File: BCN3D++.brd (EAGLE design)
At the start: 70.5 x 95.8 mm, 87 parts, among them IC2 FT232RL, Q2 IRLS3034

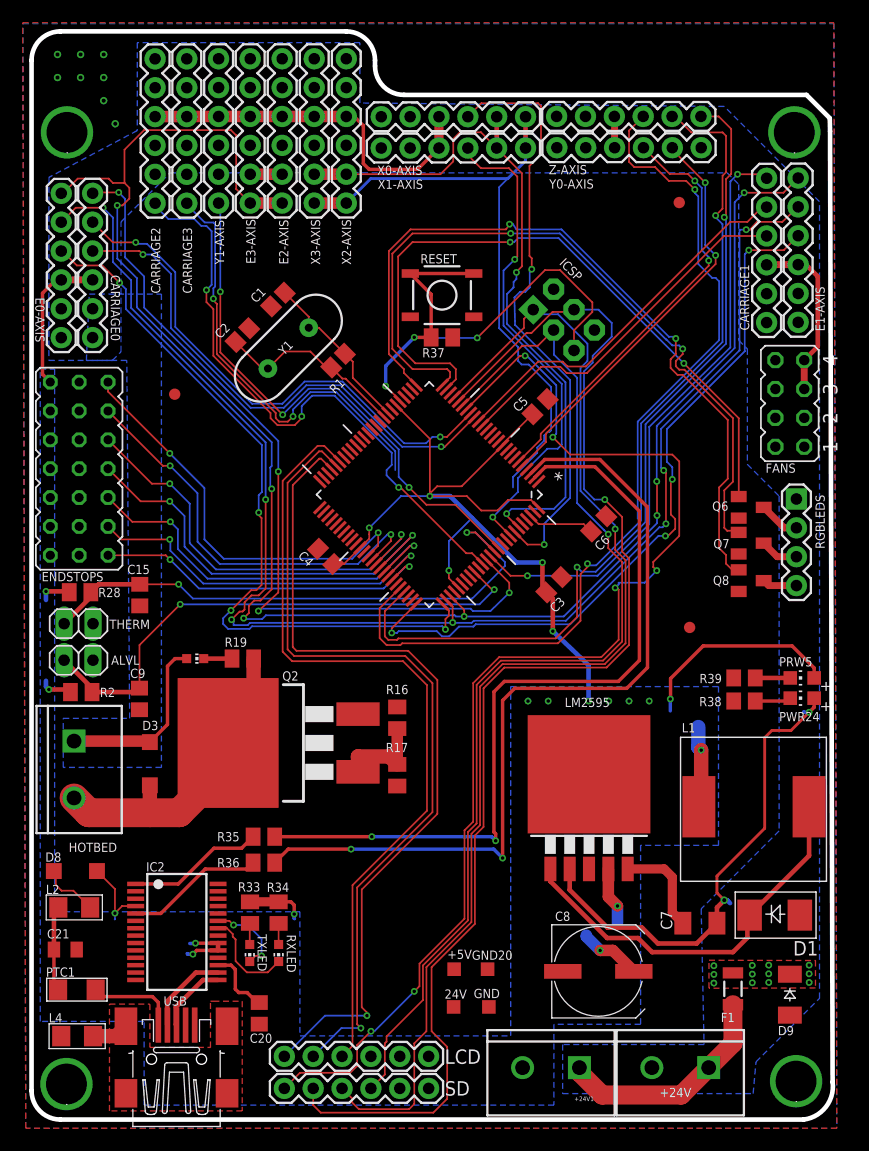
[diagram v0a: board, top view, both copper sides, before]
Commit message: Main Board almost ready
5V rail to ICSP and some headers left to connect
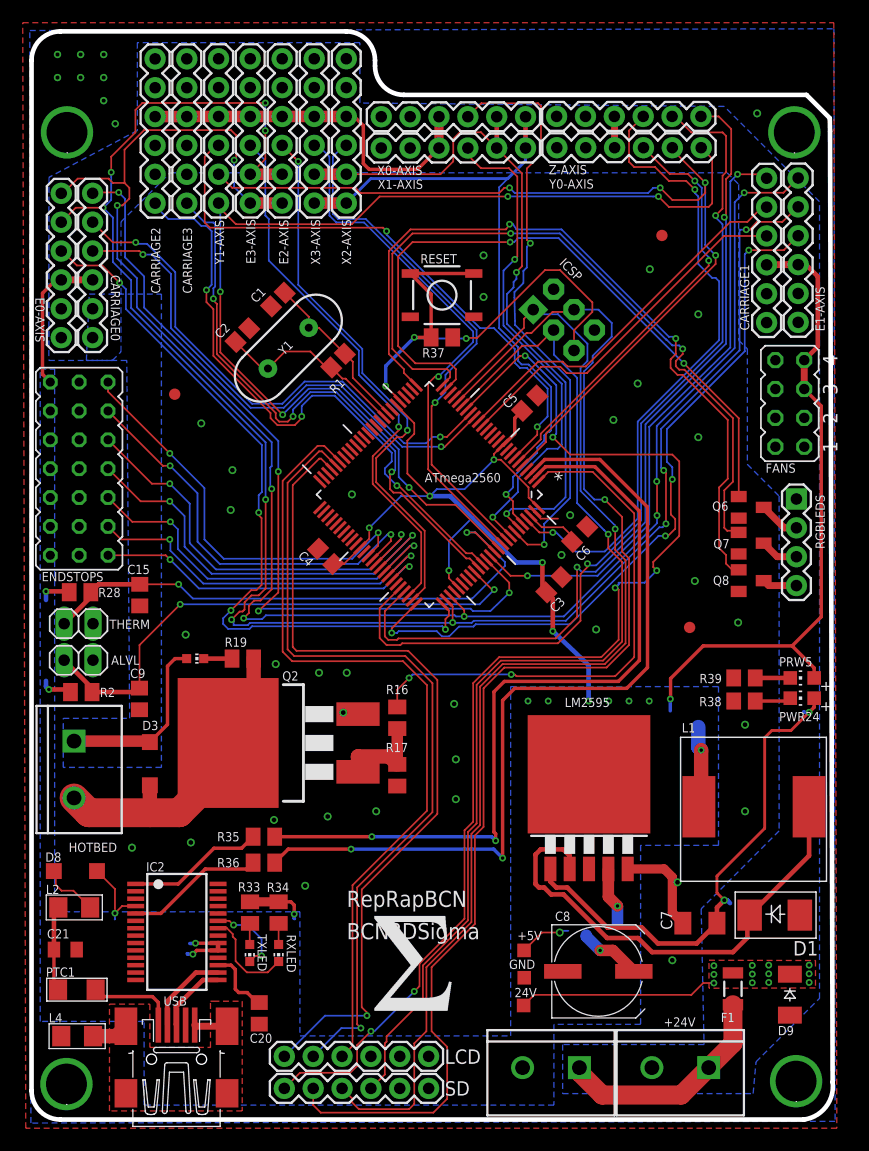
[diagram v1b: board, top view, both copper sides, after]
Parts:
- removed GND20: PTR1TP12SQ, testpad:TP12SQ
- added U$5: (no value), MarcEagleParts:SIGMA_LOGO
- moved LOGO1 63.7 mm to (27.2, 15.1)
- moved +5V 6.37 mm to (43.3, 14.9)
- moved 24V 6.16 mm to (43.3, 10.0)
- moved GND 4.03 mm to (43.4, 12.5)
- moved FID2 3.27 mm to (55.5, 77.8)
- moved C6 1.91 mm to (48.2, 51.5)
- moved C5 0.96 mm to (43.8, 63.0)
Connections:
- removed net N$128: ATMEGA2560.1
- new net 11111: ATMEGA2560.23
- net +24V: now also 24V.TP, LM2595.1; no longer LM2595.2
- net +5V: no longer 24V.TP
- net GND: no longer GND20.TP
- net N$4: now also LM2595.2; no longer LM2595.1
- net PWM_HOTBED: now also ATMEGA2560.1; no longer ATMEGA2560.23
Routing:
- net Y1-!EN: track 0.00 -> 51.8 mm, vias 0 -> 2
- net Y-STEP: track 48.1 -> 99.3 mm, vias 3 -> 5
- net E3-!EN: track 0.00 -> 48.3 mm, vias 0 -> 1
- net E2-!EN: track 0.00 -> 48.2 mm, vias 0 -> 2
- net X3-!EN: track 0.00 -> 47.0 mm, vias 0 -> 1
- net PWM_HOTBED: track 0.00 -> 46.6 mm, vias 0 -> 2
- net X2-!EN: track 0.00 -> 46.3 mm, vias 0 -> 1
- net Y-DIR: track 36.6 -> 82.3 mm, vias 2 -> 4
- net E-DIR: track 130.4 -> 158.7 mm, vias 7 -> 10
- net +5V: track 201.2 -> 226.6 mm, vias 21 -> 23
- net +24V: track 59.5 -> 78.3 mm
- net THERM3: track 38.6 -> 51.3 mm, vias 2 -> 3
- net Z-!EN: track 44.3 -> 56.4 mm, vias 1 -> 2
- net N$4: track 35.3 -> 42.6 mm
- net X-STEP: track 55.2 -> 59.3 mm, vias 0 -> 1
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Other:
- board text added: "ATmega2560"
- board text added: "RepRapBCN BCN3DSigma"
